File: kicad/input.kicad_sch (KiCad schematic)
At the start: 8 parts, among them SW601 BT1, SW602 BT2, SW603 BT3, SW604 BT4

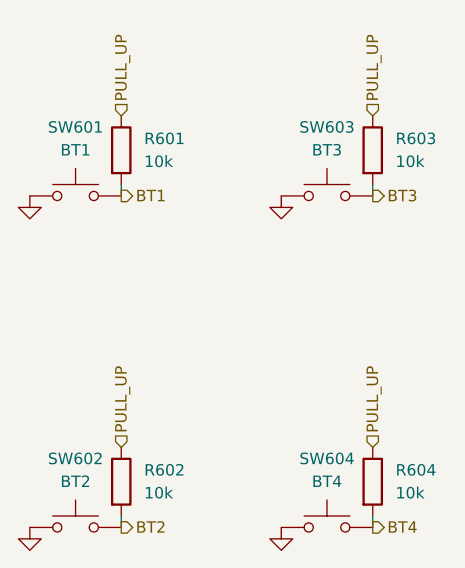
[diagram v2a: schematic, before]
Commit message: Small switch updates and fixes
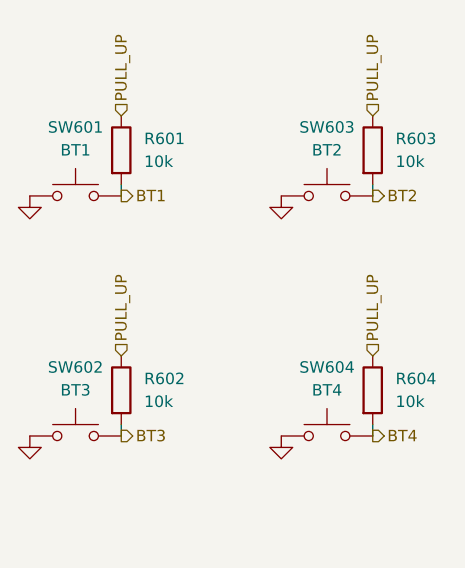
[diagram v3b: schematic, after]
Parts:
- renumbered R603 to R602, R602 to R603, SW603 to SW602, SW602 to SW603
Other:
- moved on the sheet: R602, R603, R604, SW602, SW603, SW604

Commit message: Footprint and MC updates
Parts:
- SW601, SW602, SW603, SW604: footprint Raven:PROTOTYPE_BUTTONS -> Raven:EVQPUA
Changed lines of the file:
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@@
 			)
 		)
-		(property "Footprint" "Raven:PROTOTYPE_BUTTONS"
+		(property "Footprint" "Raven:EVQPUA"
 			(at 133.35 83.82 0)
 			(effects
@@
 			)
 		)
-		(property "Footprint" "Raven:PROTOTYPE_BUTTONS"
+		(property "Footprint" "Raven:EVQPUA"
 			(at 133.35 110.49 0)
 			(effects
@@
 			)
 		)
-		(property "Footprint" "Raven:PROTOTYPE_BUTTONS"
+		(property "Footprint" "Raven:EVQPUA"
 			(at 161.29 83.82 0)
 			(effects
@@
 			)
 		)
-		(property "Footprint" "Raven:PROTOTYPE_BUTTONS"
+		(property "Footprint" "Raven:EVQPUA"
 			(at 161.29 110.49 0)
 			(effects

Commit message: Begin PCB, update footprints
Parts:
- R601, R602, R603, R604: footprint Resistor_SMD:R_0603_1608Metric_Pad0.98x0.95mm_HandSolder -> Resistor_SMD:R_0402_1005Metric
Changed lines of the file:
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@@
 			)
 		)
-		(property "Footprint" "Resistor_SMD:R_0603_1608Metric_Pad0.98x0.95mm_HandSolder"
+		(property "Footprint" "Resistor_SMD:R_0402_1005Metric"
 			(at 164.592 110.49 90)
 			(effects
@@
 			)
 		)
-		(property "Footprint" "Resistor_SMD:R_0603_1608Metric_Pad0.98x0.95mm_HandSolder"
+		(property "Footprint" "Resistor_SMD:R_0402_1005Metric"
 			(at 136.652 83.82 90)
 			(effects
@@
 			)
 		)
-		(property "Footprint" "Resistor_SMD:R_0603_1608Metric_Pad0.98x0.95mm_HandSolder"
+		(property "Footprint" "Resistor_SMD:R_0402_1005Metric"
 			(at 164.592 83.82 90)
 			(effects
@@
 			)
 		)
-		(property "Footprint" "Resistor_SMD:R_0603_1608Metric_Pad0.98x0.95mm_HandSolder"
+		(property "Footprint" "Resistor_SMD:R_0402_1005Metric"
 			(at 136.652 110.49 90)
 			(effects

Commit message: v2.0.2
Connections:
- net BT1: now also R601.1; no longer R601.2
- net BT2: now also R603.1; no longer R603.2
- net BT3: now also R602.1; no longer R602.2
- net BT4: now also R604.1; no longer R604.2
- net GND: now also R601.2, R602.2, R603.2, R604.2; no longer SW601.1, SW602.1, SW603.1, SW604.1
- net PULL_UP: now also SW601.1, SW602.1, SW603.1, SW604.1; no longer R601.1, R602.1, R603.1, R604.1
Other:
- moved on the sheet: R601, R602, R603, R604
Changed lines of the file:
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@@
 	(title_block
 		(title "Input Module")
-		(date "2025-02-03")
+		(date "2025-05-08")
 		(rev "2")
 		(company "Mosaic Labs")
 		(comment 1 "Lucas Merritt")
-		(comment 2 "Rev. 2 verified")
-		(comment 3 "Final ready")
-	)
-	(wire
-		(pts
-			(xy 138.43 114.3) (xy 138.43 115.57)
-		)
-		(stroke
-			(width 0)
-			(type default)
-		)
-	)
-	(wire
-		(pts
-			(xy 166.37 114.3) (xy 166.37 115.57)
-		)
-		(stroke
-			(width 0)
-			(type default)
-		)
-	)
-	(wire
-		(pts
-			(xy 138.43 87.63) (xy 138.43 88.9)
-		)
-		(stroke
-			(width 0)
-			(type default)
-		)
-	)
-	(wire
-		(pts
-			(xy 166.37 87.63) (xy 166.37 88.9)
-		)
-		(stroke
-			(width 0)
-			(type default)
-		)
+		(comment 2 "ACTIVE HIGH")
 	)
 	(hierarchical_label "PULL_UP"
 		(shape input)
-		(at 166.37 80.01 90)
+		(at 156.21 88.9 90)
 		(fields_autoplaced yes)
 		(effects
@@
 	(hierarchical_label "PULL_UP"
 		(shape input)
-		(at 166.37 106.68 90)
+		(at 156.21 115.57 90)
 		(fields_autoplaced yes)
 		(effects
@@
 	(hierarchical_label "PULL_UP"
 		(shape input)
-		(at 138.43 106.68 90)
+		(at 128.27 115.57 90)
 		(fields_autoplaced yes)
 		(effects
@@
 	(hierarchical_label "PULL_UP"
 		(shape input)
-		(at 138.43 80.01 90)
+		(at 128.27 88.9 90)
 		(fields_autoplaced yes)
 		(effects
@@
 	(symbol
 		(lib_id "Device:R")
-		(at 166.37 110.49 0)
+		(at 166.37 119.38 0)
 		(unit 1)
 		(exclude_from_sim no)
@@
 		(fields_autoplaced yes)
 		(property "Reference" "R604"
-			(at 168.91 109.2199 0)
+			(at 168.91 118.1099 0)
 			(effects
 				(font
@@
 		)
 		(property "Value" "10k"
-			(at 168.91 111.7599 0)
+			(at 168.91 120.6499 0)
 			(effects
 				(font
@@
 		)
 		(property "Footprint" "Resistor_SMD:R_0402_1005Metric"
-			(at 164.592 110.49 90)
+			(at 164.592 119.38 90)
 			(effects
 				(font
@@
 		)
 		(property "Datasheet" "~"
-			(at 166.37 110.49 0)
+			(at 166.37 119.38 0)
 			(effects
 				(font
@@
 		)
 		(property "Description" "Resistor"
-			(at 166.37 110.49 0)
+			(at 166.37 119.38 0)
 			(effects
 				(font
@@
 		)
 		(property "JLC" "0603"
-			(at 166.37 110.49 0)
+			(at 166.37 119.38 0)
 			(effects
 				(font
@@
 	(symbol
 		(lib_id "Device:R")
-		(at 138.43 83.82 0)
+		(at 138.43 92.71 0)
 		(unit 1)
 		(exclude_from_sim no)
@@
 		(fields_autoplaced yes)
 		(property "Reference" "R601"
-			(at 140.97 82.5499 0)
+			(at 140.97 91.4399 0)
 			(effects
 				(font
@@
 		)
 		(property "Value" "10k"
-			(at 140.97 85.0899 0)
+			(at 140.97 93.9799 0)
 			(effects
 				(font
@@
 		)
 		(property "Footprint" "Resistor_SMD:R_0402_1005Metric"
-			(at 136.652 83.82 90)
+			(at 136.652 92.71 90)
 			(effects
 				(font
@@
 		)
 		(property "Datasheet" "~"
-			(at 138.43 83.82 0)
+			(at 138.43 92.71 0)
 			(effects
 				(font
@@
 		)
 		(property "Description" "Resistor"
-			(at 138.43 83.82 0)
+			(at 138.43 92.71 0)
 			(effects
 				(font
@@
 		)
 		(property "JLC" "0603"
-			(at 138.43 83.82 0)
+			(at 138.43 92.71 0)
 			(effects
 				(font
@@
 	(symbol
 		(lib_id "power:GND")
-		(at 128.27 115.57 0)
+		(at 138.43 123.19 0)
 		(unit 1)
 		(exclude_from_sim no)
@@
 		(fields_autoplaced yes)
 		(property "Reference" "#PWR0602"
-			(at 128.27 121.92 0)
+			(at 138.43 129.54 0)
 			(effects
 				(font
@@
 		)
 		(property "Value" "GND"
-			(at 128.27 120.65 0)
+			(at 138.43 128.27 0)
 			(effects
 				(font
@@
 		)
 		(property "Footprint" ""
-			(at 128.27 115.57 0)
+			(at 138.43 123.19 0)
 			(effects
 				(font
@@
 		)
 		(property "Datasheet" ""
-			(at 128.27 115.57 0)
+			(at 138.43 123.19 0)
 			(effects
 				(font
@@
 		)
 		(property "Description" "Power symbol creates a global label with name \"GND\" , ground"
-			(at 128.27 115.57 0)
+			(at 138.43 123.19 0)
 			(effects
 				(font
@@
 	(symbol
 		(lib_id "Device:R")
-		(at 166.37 83.82 0)
+		(at 166.37 92.71 0)
 		(unit 1)
 		(exclude_from_sim no)
@@
 		(fields_autoplaced yes)
 		(property "Reference" "R603"
-			(at 168.91 82.5499 0)
+			(at 168.91 91.4399 0)
 			(effects
 				(font
@@
 		)
 		(property "Value" "10k"
-			(at 168.91 85.0899 0)
+			(at 168.91 93.9799 0)
 			(effects
 				(font
@@
 		)
 		(property "Footprint" "Resistor_SMD:R_0402_1005Metric"
-			(at 164.592 83.82 90)
+			(at 164.592 92.71 90)
 			(effects
 				(font
@@
 		)
 		(property "Datasheet" "~"
-			(at 166.37 83.82 0)
+			(at 166.37 92.71 0)
 			(effects
 				(font
@@
 		)
 		(property "Description" "Resistor"
-			(at 166.37 83.82 0)
+			(at 166.37 92.71 0)
 			(effects
 				(font
@@
 		)
 		(property "JLC" "0603"
-			(at 166.37 83.82 0)
+			(at 166.37 92.71 0)
 			(effects
 				(font
@@
 	(symbol
 		(lib_id "power:GND")
-		(at 156.21 88.9 0)
+		(at 166.37 96.52 0)
 		(unit 1)
 		(exclude_from_sim no)
@@
 		(fields_autoplaced yes)
 		(property "Reference" "#PWR0603"
-			(at 156.21 95.25 0)
+			(at 166.37 102.87 0)
 			(effects
 				(font
@@
 		)
 		(property "Value" "GND"
-			(at 156.21 93.98 0)
+			(at 166.37 101.6 0)
 			(effects
 				(font
@@
 		)
 		(property "Footprint" ""
-			(at 156.21 88.9 0)
+			(at 166.37 96.52 0)
 			(effects
 				(font
@@
 		)
 		(property "Datasheet" ""
-			(at 156.21 88.9 0)
+			(at 166.37 96.52 0)
 			(effects
 				(font
@@
 		)
 		(property "Description" "Power symbol creates a global label with name \"GND\" , ground"
-			(at 156.21 88.9 0)
+			(at 166.37 96.52 0)
 			(effects
 				(font
@@
 	(symbol
 		(lib_id "Device:R")
-		(at 138.43 110.49 0)
+		(at 138.43 119.38 0)
 		(unit 1)
 		(exclude_from_sim no)
@@
 		(fields_autoplaced yes)
 		(property "Reference" "R602"
-			(at 140.97 109.2199 0)
+			(at 140.97 118.1099 0)
 			(effects
 				(font
@@
 		)
 		(property "Value" "10k"
-			(at 140.97 111.7599 0)
+			(at 140.97 120.6499 0)
 			(effects
 				(font
@@
 		)
 		(property "Footprint" "Resistor_SMD:R_0402_1005Metric"
-			(at 136.652 110.49 90)
+			(at 136.652 119.38 90)
 			(effects
 				(font
@@
 		)
 		(property "Datasheet" "~"
-			(at 138.43 110.49 0)
+			(at 138.43 119.38 0)
 			(effects
 				(font
@@
 		)
 		(property "Description" "Resistor"
-			(at 138.43 110.49 0)
+			(at 138.43 119.38 0)
 			(effects
 				(font
@@
 		)
 		(property "JLC" "0603"
-			(at 138.43 110.49 0)
+			(at 138.43 119.38 0)
 			(effects
 				(font
@@
 	(symbol
 		(lib_id "power:GND")
-		(at 128.27 88.9 0)
+		(at 138.43 96.52 0)
 		(unit 1)
 		(exclude_from_sim no)
@@
 		(fields_autoplaced yes)
 		(property "Reference" "#PWR0601"
-			(at 128.27 95.25 0)
+			(at 138.43 102.87 0)
 			(effects
 				(font
@@
 		)
 		(property "Value" "GND"
-			(at 128.27 93.98 0)
+			(at 138.43 101.6 0)
 			(effects
 				(font
@@
 		)
 		(property "Footprint" ""
-			(at 128.27 88.9 0)
+			(at 138.43 96.52 0)
 			(effects
 				(font
@@
 		)
 		(property "Datasheet" ""
-			(at 128.27 88.9 0)
+			(at 138.43 96.52 0)
 			(effects
 				(font
@@
 		)
 		(property "Description" "Power symbol creates a global label with name \"GND\" , ground"
-			(at 128.27 88.9 0)
+			(at 138.43 96.52 0)
 			(effects
 				(font
@@
 	(symbol
 		(lib_id "power:GND")
-		(at 156.21 115.57 0)
+		(at 166.37 123.19 0)
 		(unit 1)
 		(exclude_from_sim no)
@@
 		(fields_autoplaced yes)
 		(property "Reference" "#PWR0604"
-			(at 156.21 121.92 0)
+			(at 166.37 129.54 0)
 			(effects
 				(font
@@
 		)
 		(property "Value" "GND"
-			(at 156.21 120.65 0)
+			(at 166.37 128.27 0)
 			(effects
 				(font
@@
 		)
 		(property "Footprint" ""
-			(at 156.21 115.57 0)
+			(at 166.37 123.19 0)
 			(effects
 				(font
@@
 		)
 		(property "Datasheet" ""
-			(at 156.21 115.57 0)
+			(at 166.37 123.19 0)
 			(effects
 				(font
@@
 		)
 		(property "Description" "Power symbol creates a global label with name \"GND\" , ground"
-			(at 156.21 115.57 0)
-			(effects
-				(font
+			(at 166.37 123.19 0)
+			(effects
+				(font

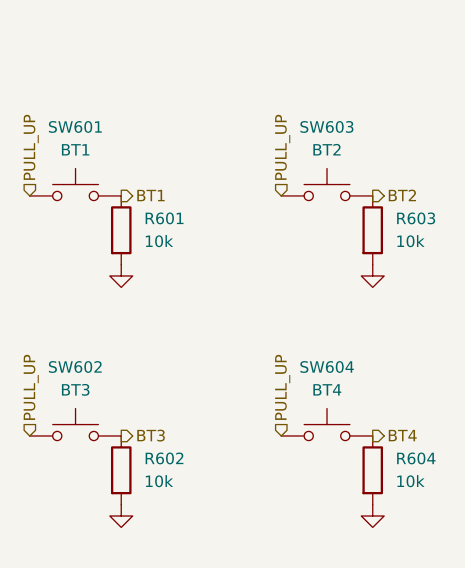
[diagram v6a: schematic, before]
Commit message: start v3, complete pcb restart and remove haptics
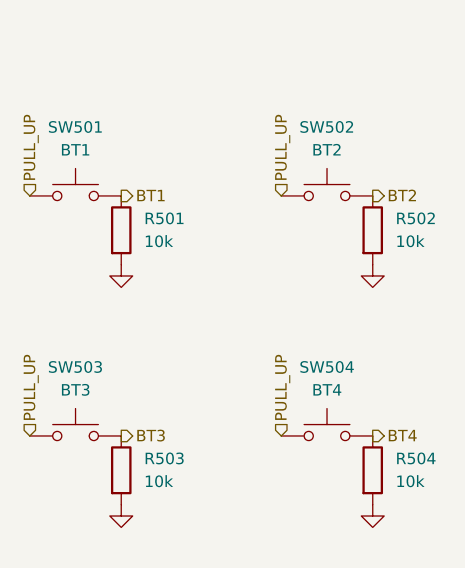
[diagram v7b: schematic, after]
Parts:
- renumbered R601 to R501, R603 to R502, R602 to R503, R604 to R504, SW601 to SW501, SW603 to SW502, SW602 to SW503, SW604 to SW504
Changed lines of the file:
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@@
 (kicad_sch
-	(version 20231120)
+	(version 20250114)
 	(generator "eeschema")
-	(generator_version "8.0")
+	(generator_version "9.0")
 	(paper "A4")
 	(title_block
@@
 		(shape input)
 		(at 156.21 88.9 90)
-		(fields_autoplaced yes)
 		(effects
 			(font
@@
 		(shape output)
 		(at 138.43 88.9 0)
-		(fields_autoplaced yes)
 		(effects
 			(font
@@
 		(shape input)
 		(at 156.21 115.57 90)
-		(fields_autoplaced yes)
 		(effects
 			(font
@@
 		(shape input)
 		(at 128.27 115.57 90)
-		(fields_autoplaced yes)
 		(effects
 			(font
@@
 		(shape output)
 		(at 166.37 88.9 0)
-		(fields_autoplaced yes)
 		(effects
 			(font
@@
 		(shape input)
 		(at 128.27 88.9 90)
-		(fields_autoplaced yes)
 		(effects
 			(font
@@
 		(shape output)
 		(at 138.43 115.57 0)
-		(fields_autoplaced yes)
 		(effects
 			(font
@@
 		(shape output)
 		(at 166.37 115.57 0)
-		(fields_autoplaced yes)
 		(effects
 			(font
@@
 		(dnp no)
 		(fields_autoplaced yes)
-		(property "Reference" "R604"
+		(property "Reference" "R504"
 			(at 168.91 118.1099 0)
 			(effects
@@
 			(project "kicad"
 				(path "/97e37379-fec6-4f0d-82d9-4ea53516bb02/61a1381c-fa91-4acb-8bba-0cebc11eb34a"
-					(reference "R604")
+					(reference "R504")
 					(unit 1)
 				)
@@
 		(dnp no)
 		(fields_autoplaced yes)
-		(property "Reference" "R601"
+		(property "Reference" "R501"
 			(at 140.97 91.4399 0)
 			(effects
@@
 			(project "kicad"
 				(path "/97e37379-fec6-4f0d-82d9-4ea53516bb02/61a1381c-fa91-4acb-8bba-0cebc11eb34a"
-					(reference "R601")
+					(reference "R501")
 					(unit 1)
 				)
@@
 		(dnp no)
 		(fields_autoplaced yes)
-		(property "Reference" "#PWR0602"
+		(property "Reference" "#PWR0503"
 			(at 138.43 129.54 0)
 			(effects
@@
 			(project "kicad"
 				(path "/97e37379-fec6-4f0d-82d9-4ea53516bb02/61a1381c-fa91-4acb-8bba-0cebc11eb34a"
-					(reference "#PWR0602")
+					(reference "#PWR0503")
 					(unit 1)
 				)
@@
 		(dnp no)
 		(fields_autoplaced yes)
-		(property "Reference" "SW601"
+		(property "Reference" "SW501"
 			(at 133.35 81.28 0)
 			(effects
@@
 			(project "kicad"
 				(path "/97e37379-fec6-4f0d-82d9-4ea53516bb02/61a1381c-fa91-4acb-8bba-0cebc11eb34a"
-					(reference "SW601")
+					(reference "SW501")
 					(unit 1)
 				)
@@
 		(dnp no)
 		(fields_autoplaced yes)
-		(property "Reference" "R603"
+		(property "Reference" "R502"
 			(at 168.91 91.4399 0)
 			(effects
@@
 			(project "kicad"
 				(path "/97e37379-fec6-4f0d-82d9-4ea53516bb02/61a1381c-fa91-4acb-8bba-0cebc11eb34a"
-					(reference "R603")
+					(reference "R502")
 					(unit 1)
 				)
@@
 		(dnp no)
 		(fields_autoplaced yes)
-		(property "Reference" "#PWR0603"
+		(property "Reference" "#PWR0502"
 			(at 166.37 102.87 0)
 			(effects
@@
 			(project "kicad"
 				(path "/97e37379-fec6-4f0d-82d9-4ea53516bb02/61a1381c-fa91-4acb-8bba-0cebc11eb34a"
-					(reference "#PWR0603")
+					(reference "#PWR0502")
 					(unit 1)
 				)
@@
 		(dnp no)
 		(fields_autoplaced yes)
-		(property "Reference" "SW602"
+		(property "Reference" "SW503"
 			(at 133.35 107.95 0)
 			(effects
@@
 			(project "kicad"
 				(path "/97e37379-fec6-4f0d-82d9-4ea53516bb02/61a1381c-fa91-4acb-8bba-0cebc11eb34a"
-					(reference "SW602")
+					(reference "SW503")
 					(unit 1)
 				)
@@
 		(dnp no)
 		(fields_autoplaced yes)
-		(property "Reference" "R602"
+		(property "Reference" "R503"
 			(at 140.97 118.1099 0)
 			(effects
@@
 			(project "kicad"
 				(path "/97e37379-fec6-4f0d-82d9-4ea53516bb02/61a1381c-fa91-4acb-8bba-0cebc11eb34a"
-					(reference "R602")
+					(reference "R503")
 					(unit 1)
 				)
@@
 		(dnp no)
 		(fields_autoplaced yes)
-		(property "Reference" "#PWR0601"
+		(property "Reference" "#PWR0501"
 			(at 138.43 102.87 0)
 			(effects
@@
 			(project "kicad"
 				(path "/97e37379-fec6-4f0d-82d9-4ea53516bb02/61a1381c-fa91-4acb-8bba-0cebc11eb34a"
-					(reference "#PWR0601")
+					(reference "#PWR0501")
 					(unit 1)
 				)
@@
 		(dnp no)
 		(fields_autoplaced yes)
-		(property "Reference" "SW603"
+		(property "Reference" "SW502"
 			(at 161.29 81.28 0)
 			(effects
@@
 			(project "kicad"
 				(path "/97e37379-fec6-4f0d-82d9-4ea53516bb02/61a1381c-fa91-4acb-8bba-0cebc11eb34a"
-					(reference "SW603")
+					(reference "SW502")
 					(unit 1)
 				)
@@
 		(dnp no)
 		(fields_autoplaced yes)
-		(property "Reference" "#PWR0604"
+		(property "Reference" "#PWR0504"
 			(at 166.37 129.54 0)
 			(effects
@@
 			(project "kicad"
 				(path "/97e37379-fec6-4f0d-82d9-4ea53516bb02/61a1381c-fa91-4acb-8bba-0cebc11eb34a"
-					(reference "#PWR0604")
+					(reference "#PWR0504")
 					(unit 1)
 				)
@@
 		(dnp no)
 		(fields_autoplaced yes)
-		(property "Reference" "SW604"
+		(property "Reference" "SW504"
 			(at 161.29 107.95 0)
 			(effects
@@
 			(project "kicad"
 				(path "/97e37379-fec6-4f0d-82d9-4ea53516bb02/61a1381c-fa91-4acb-8bba-0cebc11eb34a"
-					(reference "SW604")
-					(unit 1)
-				)
+					(reference "SW504")
+					(unit 1)
+				)
